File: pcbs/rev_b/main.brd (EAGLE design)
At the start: 91.9 x 56.4 mm, 20 parts

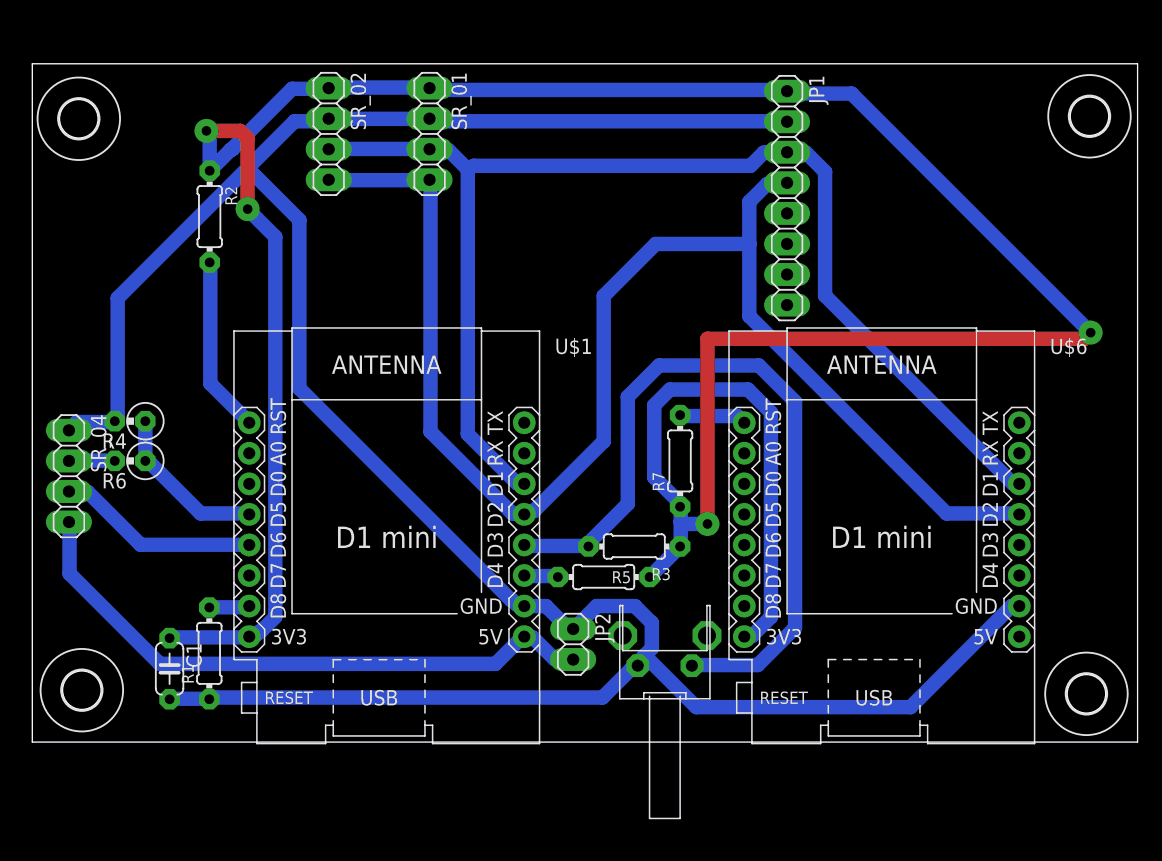
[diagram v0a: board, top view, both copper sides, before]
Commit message: rev.b board updates - add more I2C busses for expansion - Add 5v power jumpers for expansion - Motor controller is now powered by 5v line from circuit board (less wires)
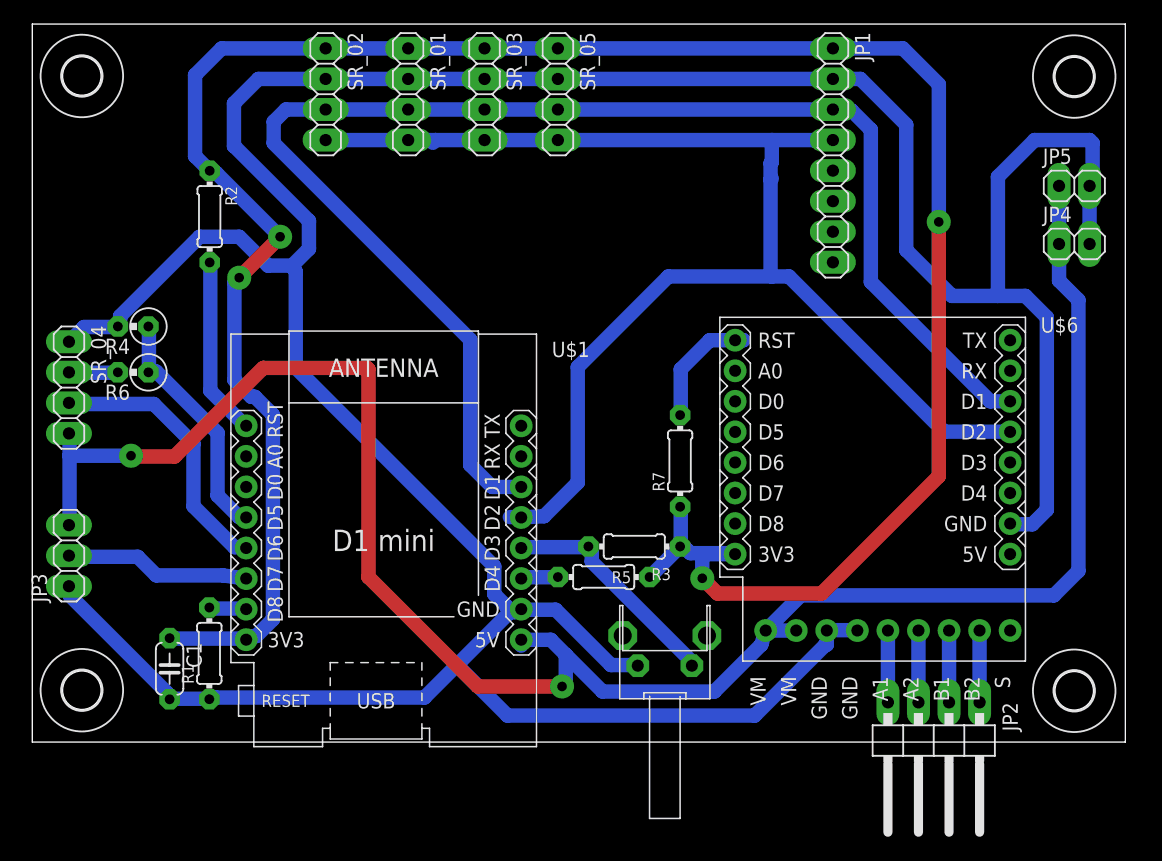
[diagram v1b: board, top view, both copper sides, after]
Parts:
- added JP3: (no value), pinhead:1X03
- added JP4, JP5: (no value), pinhead:1X02
- added SR_03, SR_05: (no value), pinhead:1X04
- JP2: device pinhead:1X02 -> pinhead:1X04/90
- U$6: value WEMOS-D1-MINI -> WEMOS-D1-MINI-SHIELDWEMOS-MOTOR-SHIELD; device diy-modules:WEMOS-D1-MINI -> glowmouse_custom:WEMOS-D1-MINI-SHIELD
- moved JP2 31.2 mm to (74.9, -0.51), turned to 180 degrees
- moved R4 7.88 mm to (8.38, 34.5)
- moved R6 7.37 mm to (8.38, 30.7)
- moved SR_04 7.37 mm to (3.05, 29.5)
- moved JP1 5.21 mm to (66.5, 48.8)
- moved U$6 4.38 mm to (69.8, 21.3)
- moved SR_01 3.75 mm to (31.2, 53.8)
- moved U$4 3.57 mm to (4.12, 55.4)
- moved U$3 3.54 mm to (86.6, 55.3)
- moved SR_02 3.31 mm to (24.4, 53.8)
- moved U$5 1.05 mm to (86.6, 4.26)
- moved U$1 0.36 mm to (29.2, 16.8)
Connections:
- new net N$1: JP2.4, U$6.A1
- new net N$10: JP2.3, U$6.A2
- new net N$16: JP2.2, U$6.B1
- new net N$17: JP2.1, U$6.B2
- new net N$20: JP3.2, U$1.JP1.6
- net N$2: now also JP3.1, JP4.2, JP5.2, SR_03.2, SR_05.2, U$6.MGND1, U$6.MGND2; no longer JP2.1
- net N$3: now also SR_03.3, SR_05.3
- net N$4: now also SR_03.4, SR_05.4
- net N$6: now also JP3.3, JP4.1, JP5.1, U$6.VM1, U$6.VM2; no longer JP2.2
- net N$8: now also SR_03.1, SR_05.1
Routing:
- net N$6: track 51.0 -> 164.5 mm, vias 0 -> 2
- net N$2: track 215.7 -> 301.6 mm
- net N$18: track 64.1 -> 19.1 mm
- net N$8: track 239.8 -> 198.7 mm
- net N$3: track 104.5 -> 120.7 mm
- net N$20: track 0.00 -> 15.4 mm
- net N$13: track 13.8 -> 20.0 mm
- net N$17: track 0.00 -> 6.11 mm
- net N$11: track 16.8 -> 22.8 mm
- net N$16: track 0.00 -> 5.97 mm
- net N$10: track 0.00 -> 5.97 mm
- net N$1: track 0.00 -> 5.97 mm
- net N$5: track 5.60 -> 10.7 mm
- net N$4: track 117.7 -> 118.2 mm
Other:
- board size 91.9 x 56.4 mm -> 90.9 x 59.7 mm

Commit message: Update rev2 circuit board
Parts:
- removed SR_01, SR_02, SR_03, SR_04, SR_05: (no value), pinhead:1X04
- added JP10, JP11, JP6, JP7, JP8, JP9: (no value), pinhead:1X04
- moved R6 13.0 mm to (8.13, 43.7)
- moved R4 11.4 mm to (8.13, 46.0)
- moved JP3 2.54 mm to (3.05, 13.0)
- moved C1 1.52 mm to (12.9, 6.10)
- moved R1 0.51 mm to (15.2, 7.37)
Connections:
- removed net N$2: C1.2, JP1.2, JP3.1, JP4.2, JP5.2, R1.1, R4.2, SR_01.2, SR_02.2, SR_03.2, SR_04.1, SR_05.2, U$1.JP2.7, U$6.JP2.7, U$6.MGND1, U$6.MGND2, U$7.PB_P0
- removed net N$3: JP1.3, SR_01.3, SR_02.3, SR_03.3, SR_05.3, U$1.JP2.3, U$6.JP2.3
- removed net N$4: JP1.4, SR_01.4, SR_02.4, SR_03.4, SR_05.4, U$1.JP2.4, U$6.JP2.4
- removed net N$8: C1.1, JP1.1, R2.1, R3.1, R5.1, R7.1, SR_01.1, SR_02.1, SR_03.1, SR_05.1, U$1.JP1.8, U$6.JP1.8
- new net N$19: JP7.2, U$1.JP1.3
- new net N$21: C1.1, JP1.1, JP10.1, JP11.1, JP6.4, JP8.4, JP9.4, R2.1, R3.1, R5.1, R7.1, U$1.JP1.8, U$6.JP1.8
- new net N$22: C1.2, JP1.2, JP10.2, JP11.2, JP3.1, JP4.2, JP5.2, JP6.3, JP7.4, JP8.3, JP9.3, R1.1, R4.2, U$1.JP2.7, U$6.JP2.7, U$6.MGND1, U$6.MGND2, U$7.PB_P0
- new net N$23: JP1.3, JP10.3, JP11.3, JP8.2, JP9.2, U$1.JP2.3, U$6.JP2.3
- new net N$24: JP1.4, JP10.4, JP11.4, JP8.1, JP9.1, U$1.JP2.4, U$6.JP2.4
- net N$11: now also JP6.2; no longer SR_04.3
- net N$15: now also JP3.2
- net N$20: now also JP6.1; no longer JP3.2
- net N$6: now also JP7.1; no longer SR_04.4
- net N$9: now also JP7.3; no longer SR_04.2
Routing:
- net N$22: track 0.00 -> 330.3 mm, vias 0 -> 2
- net N$2: track 301.6 -> 0.00 mm
- net N$21: track 0.00 -> 230.7 mm, vias 0 -> 6
- net N$8: track 198.7 -> 0.00 mm, vias 4 -> 0
- net N$3: track 120.7 -> 0.00 mm
- net N$23: track 0.00 -> 120.1 mm
- net N$4: track 118.2 -> 0.00 mm
- net N$24: track 0.00 -> 109.5 mm
- net N$19: track 0.00 -> 30.0 mm, vias 0 -> 2
- net N$6: track 164.5 -> 180.0 mm
- net N$15: track 3.11 -> 15.5 mm
- net N$13: track 20.0 -> 32.4 mm
- net N$11: track 22.8 -> 14.3 mm
- net N$20: track 15.4 -> 13.1 mm
